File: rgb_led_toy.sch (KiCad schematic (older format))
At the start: 36 parts, among them IC1 AT168, IC2 MBI5168, P1 CONN_4, P2 CONN_4, P3 CONN_6, Q1 IRLML 2502 P-FET, Q2 IRLML 2502 P-FET, Q3 IRLML 2502 P-FET

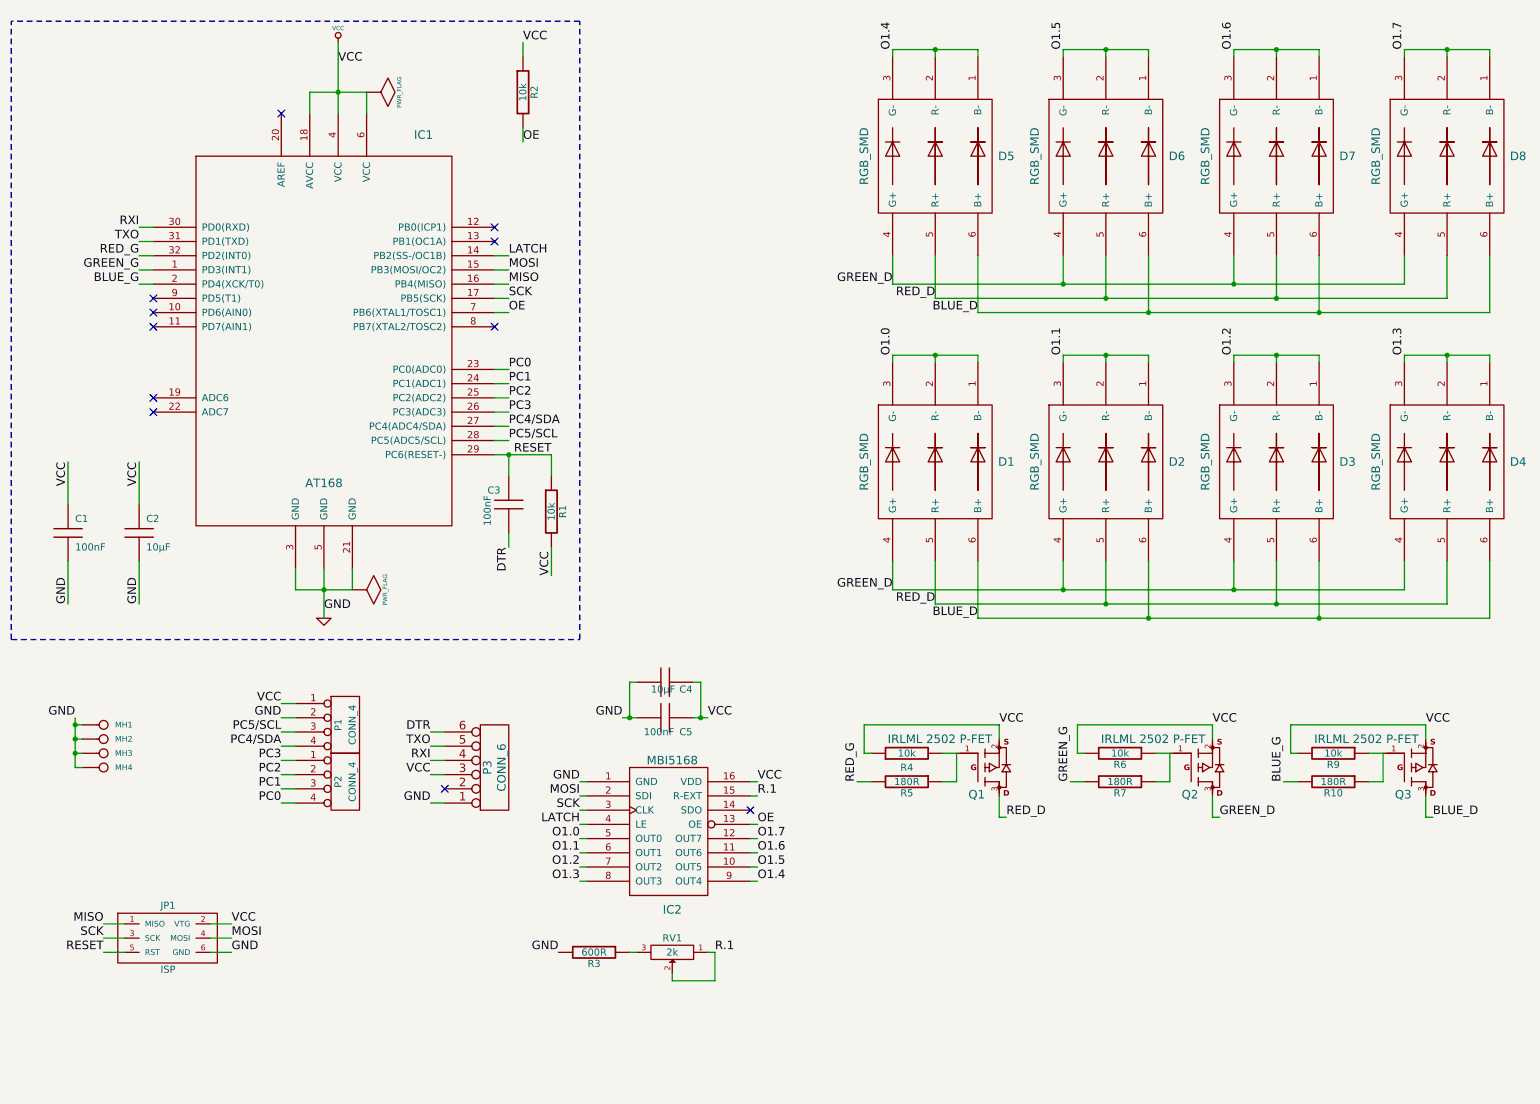
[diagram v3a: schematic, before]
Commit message: Routed V2.0 beta with 3x MBI5168 instead of just one + 3 P-FETs.
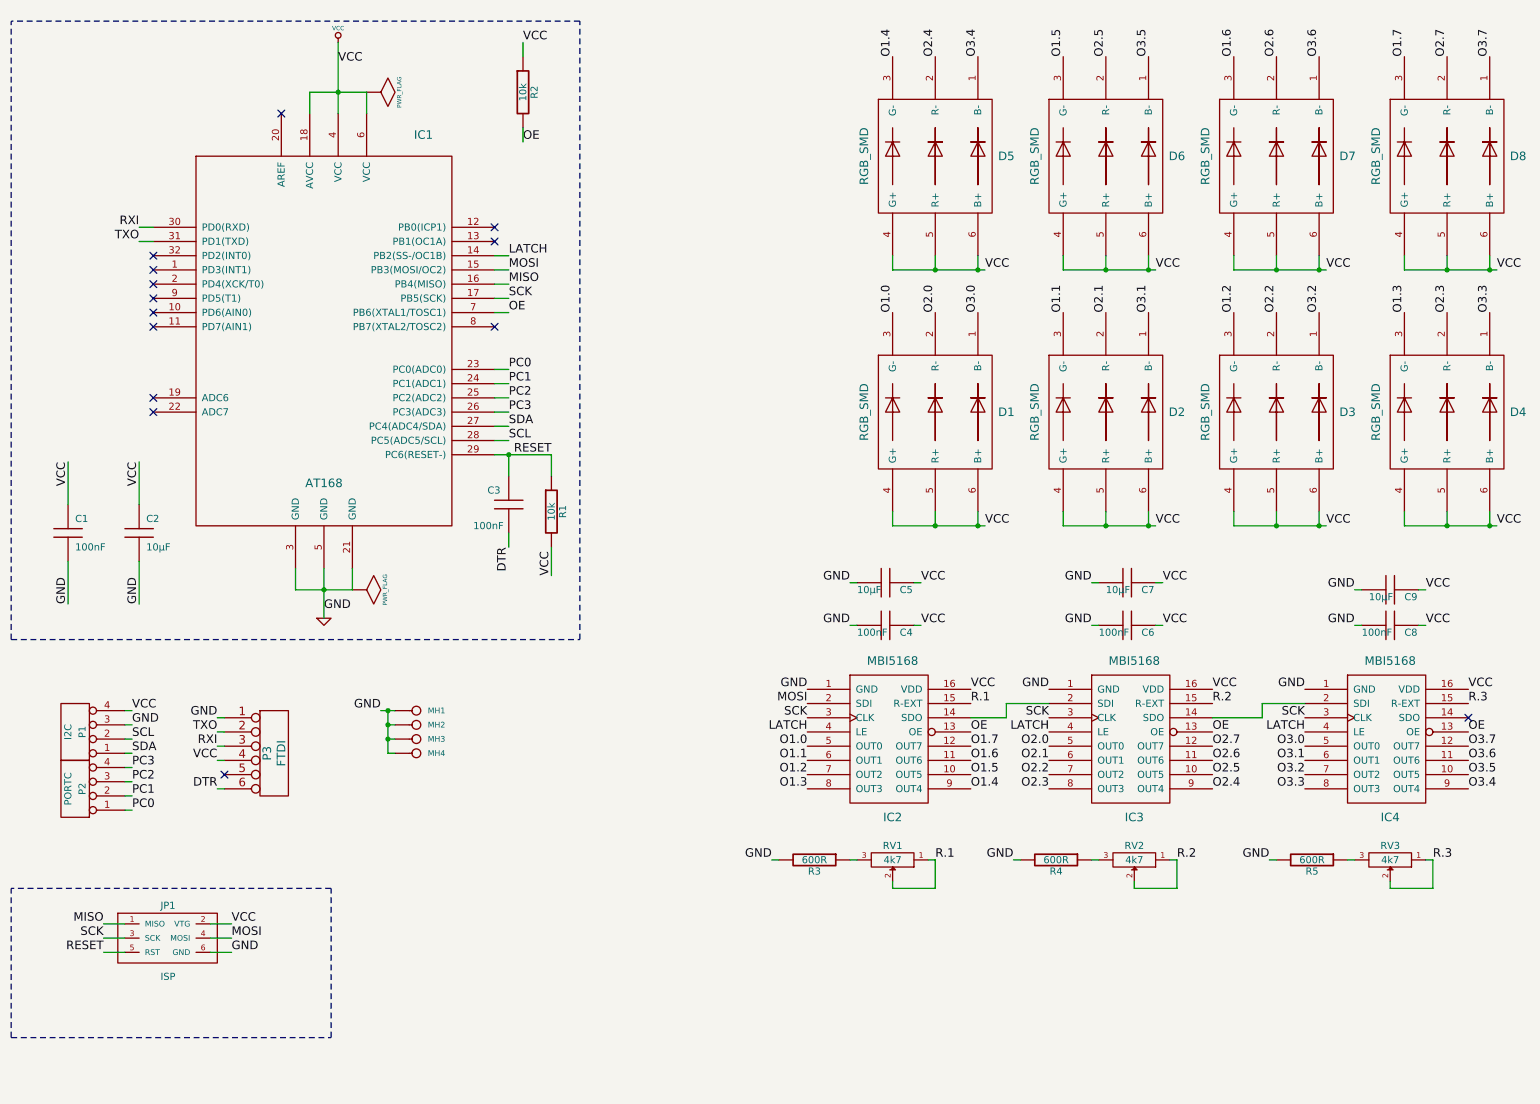
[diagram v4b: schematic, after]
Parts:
- removed C4: 10µF, symbol C
- removed Q1, Q2, Q3: IRLML 2502 P-FET, symbol MOSFET_P
- removed R10, R7: 180R, symbol R
- removed R6, R9: 10k, symbol R
- added C5, C7, C9: 10µF, symbol C
- added C6, C8: 100nF, symbol C
- added IC3, IC4: MBI5168, symbol MBI5168
- added RV2, RV3: 4k7, symbol POT
- P1: value CONN_4 -> I2C
- P2: value CONN_4 -> PORTC
- P3: value CONN_6 -> FTDI
- R4: value 10k -> 600R
- R5: value 180R -> 600R
- RV1: value 2k -> 4k7
- renumbered C5 to C4
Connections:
- net BLUE_D is gone; now on net VCC: D1.6 (B+), D2.6 (B+), D3.6 (B+), D4.6 (B+), D5.6 (B+), D6.6 (B+), D7.6 (B+), D8.6 (B+)
- net GREEN_D is gone; now on net VCC: D1.4 (G+), D2.4 (G+), D3.4 (G+), D4.4 (G+), D5.4 (G+), D6.4 (G+), D7.4 (G+), D8.4 (G+)
- net RED_D is gone; now on net VCC: D1.5 (R+), D2.5 (R+), D3.5 (R+), D4.5 (R+), D5.5 (R+), D6.5 (R+), D7.5 (R+), D8.5 (R+)
- net GND: now also P1.3 (P3), R4.2, R5.2, C5.2, C6.2, C7.2, C8.2, C9.2, IC3.1 (GND), IC4.1 (GND); no longer P1.2 (P2)
- net LATCH: now also IC3.4 (LE), IC4.4 (LE)
- net O1.0: no longer D1.1 (B-), D1.2 (R-)
- net O1.1: no longer D2.1 (B-), D2.2 (R-)
- net O1.2: no longer D3.1 (B-), D3.2 (R-)
- net O1.3: no longer D4.1 (B-), D4.2 (R-)
- net O1.4: no longer D5.1 (B-), D5.2 (R-)
- net O1.5: no longer D6.1 (B-), D6.2 (R-)
- net O1.6: no longer D7.1 (B-), D7.2 (R-)
- net O1.7: no longer D8.1 (B-), D8.2 (R-)
- net OE: now also IC3.13 (OE), IC4.13 (OE)
- net PC0: now also P2.1 (P1); no longer P2.4 (P4)
- net PC1: now also P2.2 (P2); no longer P2.3 (P3)
- net PC2: now also P2.3 (P3); no longer P2.2 (P2)
- net PC3: now also P2.4 (P4); no longer P2.1 (P1)
- net RXI: now also P3.3; no longer P3.4
- net SCK: now also IC3.3 (CLK), IC4.3 (CLK)
- net TXO: now also P3.2; no longer P3.5
- net VCC: now also P1.4 (P4), P3.4, C5.1, C6.1, C7.1, C8.1, C9.1, IC3.16 (VDD), IC4.16 (VDD); no longer P1.1 (P1), P3.3, R4.1
- net at IC2.14 (SDO): now also IC3.2 (SDI)
- net at R5.1: now also RV3.3; no longer R4.2
- net BLUE_G: no longer names the net of IC1.2 (PD4(XCK/T0))
- net GREEN_G: no longer names the net of IC1.1 (PD3(INT1))
- net PC4/SDA renamed SDA
- net SDA: now also P1.1 (P1); no longer P1.4 (P4)
- net PC5/SCL renamed SCL
- net SCL: now also P1.2 (P2); no longer P1.3 (P3)
- net RED_G: no longer names the net of IC1.32 (PD2(INT0))
- net RED_G: no longer R5.2
- new net: IC3.14 (SDO), IC4.2 (SDI)
- new net: R4.1, RV2.3
- new net O2.0: D1.2 (R-), IC3.5 (OUT0)
- new net O2.1: D2.2 (R-), IC3.6 (OUT1)
- new net O2.2: D3.2 (R-), IC3.7 (OUT2)
- new net O2.3: D4.2 (R-), IC3.8 (OUT3)
- new net O2.4: D5.2 (R-), IC3.9 (OUT4)
- new net O2.5: D6.2 (R-), IC3.10 (OUT5)
- new net O2.6: D7.2 (R-), IC3.11 (OUT6)
- new net O2.7: D8.2 (R-), IC3.12 (OUT7)
- new net O3.0: D1.1 (B-), IC4.5 (OUT0)
- new net O3.1: D2.1 (B-), IC4.6 (OUT1)
- new net O3.2: D3.1 (B-), IC4.7 (OUT2)
- new net O3.3: D4.1 (B-), IC4.8 (OUT3)
- new net O3.4: D5.1 (B-), IC4.9 (OUT4)
- new net O3.5: D6.1 (B-), IC4.10 (OUT5)
- new net O3.6: D7.1 (B-), IC4.11 (OUT6)
- new net O3.7: D8.1 (B-), IC4.12 (OUT7)
- new net R.2: IC3.15 (R-EXT), RV2.1, RV2.2
- new net R.3: IC4.15 (R-EXT), RV3.1, RV3.2
- no-connect marks 11 -> 14
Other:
- moved on the sheet: C4, D1, D2, D3, D4, IC2, MH1, MH2, MH3, MH4, R3, RV1
